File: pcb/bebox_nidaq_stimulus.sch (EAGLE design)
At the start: 4 parts, among them J1 SJ-435107RS, J6 SJ-435107RS, U1 MCP23008-E/P, X1 71430-0101

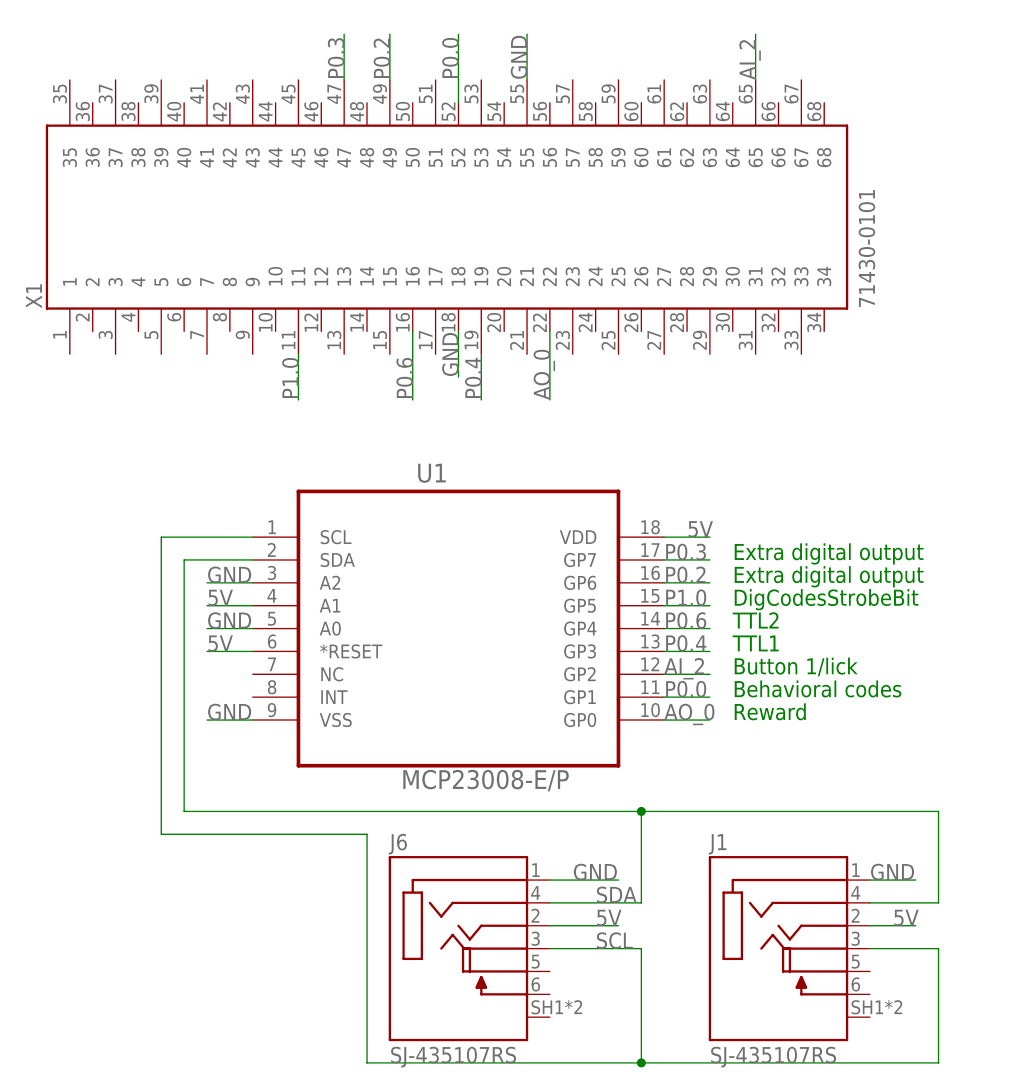
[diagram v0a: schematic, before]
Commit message: Reorderd pins so that they would be more general across users.
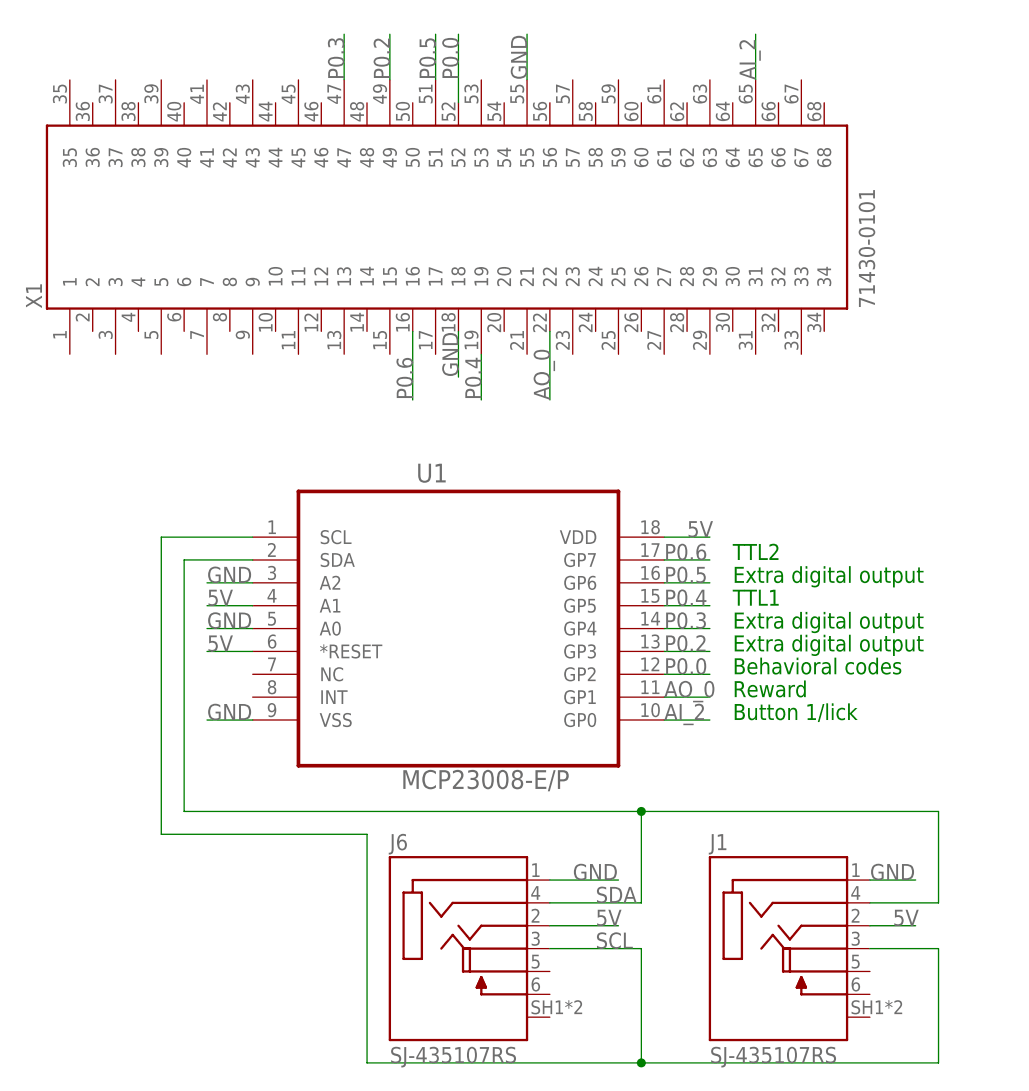
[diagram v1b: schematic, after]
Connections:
- removed net P1.0: U1.GP5, X1.11
- new net P0.5: U1.GP6, X1.51
- net AI_2: now also U1.GP0; no longer U1.GP2
- net AO_0: now also U1.GP1; no longer U1.GP0
- net P0.0: now also U1.GP2; no longer U1.GP1
- net P0.2: now also U1.GP3; no longer U1.GP6
- net P0.3: now also U1.GP4; no longer U1.GP7
- net P0.4: now also U1.GP5; no longer U1.GP3
- net P0.6: now also U1.GP7; no longer U1.GP4
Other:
- note removed: "DigCodesStrobeBit"
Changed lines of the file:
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@@
 <sheet>
 <plain>
-<text x="104.14" y="40.64" size="1.778" layer="91">Reward</text>
-<text x="104.14" y="43.18" size="1.778" layer="91">Behavioral codes</text>
-<text x="104.14" y="45.72" size="1.778" layer="91">Button 1/lick</text>
-<text x="104.14" y="48.26" size="1.778" layer="91">TTL1</text>
-<text x="104.14" y="50.8" size="1.778" layer="91">TTL2</text>
-<text x="104.14" y="53.34" size="1.778" layer="91">DigCodesStrobeBit</text>
+<text x="104.14" y="43.18" size="1.778" layer="91">Reward</text>
+<text x="104.14" y="45.72" size="1.778" layer="91">Behavioral codes</text>
+<text x="104.14" y="40.64" size="1.778" layer="91">Button 1/lick</text>
+<text x="104.14" y="53.34" size="1.778" layer="91">TTL1</text>
+<text x="104.14" y="58.42" size="1.778" layer="91">TTL2</text>
 <text x="104.14" y="55.88" size="1.778" layer="91">Extra digital output</text>
-<text x="104.14" y="58.42" size="1.778" layer="91">Extra digital output</text>
+<text x="104.14" y="48.26" size="1.778" layer="91">Extra digital output</text>
+<text x="104.14" y="50.8" size="1.778" layer="91">Extra digital output</text>
 </plain>
 <instances>
@@
 </segment>
 <segment>
+<pinref part="U1" gate="A" pin="GP1"/>
+<wire x1="96.52" y1="43.18" x2="101.6" y2="43.18" width="0.1524" layer="91"/>
+<label x="96.52" y="43.18" size="1.778" layer="95"/>
+</segment>
+</net>
+<net name="P0.0" class="0">
+<segment>
+<pinref part="X1" gate="G$1" pin="52"/>
+<wire x1="73.66" y1="109.22" x2="73.66" y2="116.84" width="0.1524" layer="91"/>
+<label x="73.66" y="111.76" size="1.778" layer="95" rot="R90"/>
+</segment>
+<segment>
+<pinref part="U1" gate="A" pin="GP2"/>
+<wire x1="96.52" y1="45.72" x2="101.6" y2="45.72" width="0.1524" layer="91"/>
+<label x="96.52" y="45.72" size="1.778" layer="95"/>
+</segment>
+</net>
+<net name="AI_2" class="0">
+<segment>
+<pinref part="X1" gate="G$1" pin="65"/>
+<wire x1="106.68" y1="111.76" x2="106.68" y2="116.84" width="0.1524" layer="91"/>
+<label x="106.68" y="111.76" size="1.778" layer="95" rot="R90"/>
+</segment>
+<segment>
 <pinref part="U1" gate="A" pin="GP0"/>
 <wire x1="96.52" y1="40.64" x2="101.6" y2="40.64" width="0.1524" layer="91"/>
@@
 </segment>
 </net>
-<net name="P0.0" class="0">
-<segment>
-<pinref part="X1" gate="G$1" pin="52"/>
-<wire x1="73.66" y1="109.22" x2="73.66" y2="116.84" width="0.1524" layer="91"/>
-<label x="73.66" y="111.76" size="1.778" layer="95" rot="R90"/>
-</segment>
-<segment>
-<pinref part="U1" gate="A" pin="GP1"/>
-<wire x1="96.52" y1="43.18" x2="101.6" y2="43.18" width="0.1524" layer="91"/>
-<label x="96.52" y="43.18" size="1.778" layer="95"/>
-</segment>
-</net>
-<net name="AI_2" class="0">
-<segment>
-<pinref part="U1" gate="A" pin="GP2"/>
-<wire x1="96.52" y1="45.72" x2="101.6" y2="45.72" width="0.1524" layer="91"/>
-<label x="96.52" y="45.72" size="1.778" layer="95"/>
-</segment>
-<segment>
-<pinref part="X1" gate="G$1" pin="65"/>
-<wire x1="106.68" y1="111.76" x2="106.68" y2="116.84" width="0.1524" layer="91"/>
-<label x="106.68" y="111.76" size="1.778" layer="95" rot="R90"/>
-</segment>
-</net>
 <net name="P0.4" class="0">
 <segment>
@@
 </segment>
 <segment>
+<pinref part="U1" gate="A" pin="GP5"/>
+<wire x1="96.52" y1="53.34" x2="101.6" y2="53.34" width="0.1524" layer="91"/>
+<label x="96.52" y="53.34" size="1.778" layer="95"/>
+</segment>
+</net>
+<net name="P0.6" class="0">
+<segment>
+<pinref part="X1" gate="G$1" pin="16"/>
+<wire x1="68.58" y1="83.82" x2="68.58" y2="76.2" width="0.1524" layer="91"/>
+<label x="68.58" y="76.2" size="1.778" layer="95" rot="R90"/>
+</segment>
+<segment>
+<pinref part="U1" gate="A" pin="GP7"/>
+<wire x1="96.52" y1="58.42" x2="101.6" y2="58.42" width="0.1524" layer="91"/>
+<label x="96.52" y="58.42" size="1.778" layer="95"/>
+</segment>
+</net>
+<net name="P0.2" class="0">
+<segment>
+<pinref part="X1" gate="G$1" pin="49"/>
+<wire x1="66.04" y1="111.76" x2="66.04" y2="116.84" width="0.1524" layer="91"/>
+<label x="66.04" y="111.76" size="1.778" layer="95" rot="R90"/>
+</segment>
+<segment>
 <pinref part="U1" gate="A" pin="GP3"/>
 <wire x1="96.52" y1="48.26" x2="101.6" y2="48.26" width="0.1524" layer="91"/>
@@
 </segment>
 </net>
-<net name="P0.6" class="0">
-<segment>
-<pinref part="X1" gate="G$1" pin="16"/>
-<wire x1="68.58" y1="83.82" x2="68.58" y2="76.2" width="0.1524" layer="91"/>
-<label x="68.58" y="76.2" size="1.778" layer="95" rot="R90"/>
+<net name="P0.3" class="0">
+<segment>
+<pinref part="X1" gate="G$1" pin="47"/>
+<wire x1="60.96" y1="111.76" x2="60.96" y2="116.84" width="0.1524" layer="91"/>
+<label x="60.96" y="111.76" size="1.778" layer="95" rot="R90"/>
 </segment>
 <segment>
@@
 </segment>
 </net>
-<net name="P1.0" class="0">
-<segment>
-<pinref part="X1" gate="G$1" pin="11"/>
-<wire x1="55.88" y1="81.28" x2="55.88" y2="76.2" width="0.1524" layer="91"/>
-<label x="55.88" y="76.2" size="1.778" layer="95" rot="R90"/>
-</segment>
-<segment>
-<pinref part="U1" gate="A" pin="GP5"/>
-<wire x1="96.52" y1="53.34" x2="101.6" y2="53.34" width="0.1524" layer="91"/>
-<label x="96.52" y="53.34" size="1.778" layer="95"/>
-</segment>
-</net>
-<net name="P0.2" class="0">
-<segment>
-<pinref part="X1" gate="G$1" pin="49"/>
-<wire x1="66.04" y1="111.76" x2="66.04" y2="116.84" width="0.1524" layer="91"/>
-<label x="66.04" y="111.76" size="1.778" layer="95" rot="R90"/>
-</segment>
+<net name="P0.5" class="0">
 <segment>
 <pinref part="U1" gate="A" pin="GP6"/>
@@
 <label x="96.52" y="55.88" size="1.778" layer="95"/>
 </segment>
-</net>
-<net name="P0.3" class="0">
-<segment>
-<pinref part="X1" gate="G$1" pin="47"/>
-<wire x1="60.96" y1="111.76" x2="60.96" y2="116.84" width="0.1524" layer="91"/>
-<label x="60.96" y="111.76" size="1.778" layer="95" rot="R90"/>
-</segment>
-<segment>
-<pinref part="U1" gate="A" pin="GP7"/>
-<wire x1="96.52" y1="58.42" x2="101.6" y2="58.42" width="0.1524" layer="91"/>
-<label x="96.52" y="58.42" size="1.778" layer="95"/>
-</segment>
-</net>
+<segment>
+<pinref part="X1" gate="G$1" pin="51"/>
+<wire x1="71.12" y1="111.76" x2="71.12" y2="116.84" width="0.1524" layer="91"/>
+<label x="71.12" y="111.76" size="1.778" layer="95" rot="R90"/>
+</segment>
+</net>
